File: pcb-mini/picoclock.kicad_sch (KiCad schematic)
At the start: 74 parts, among them J1 UART, J10 USB, J11 Alt Power, J12 LED_5V, J14 SJ2-35863B1-SMT-TR, J2 USB_A, J3 UART, J4 xx, J5 Micro_SD_Card_Det1, J6 USB_C_Receptacle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

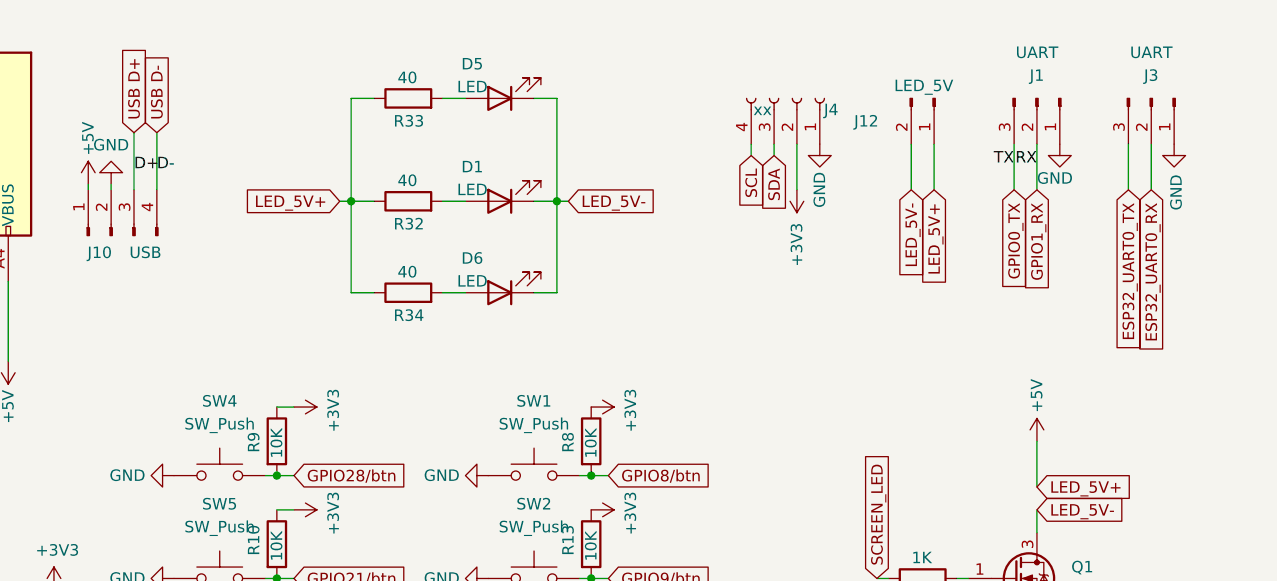
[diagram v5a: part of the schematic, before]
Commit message: [pcb] mini: add RGB leds
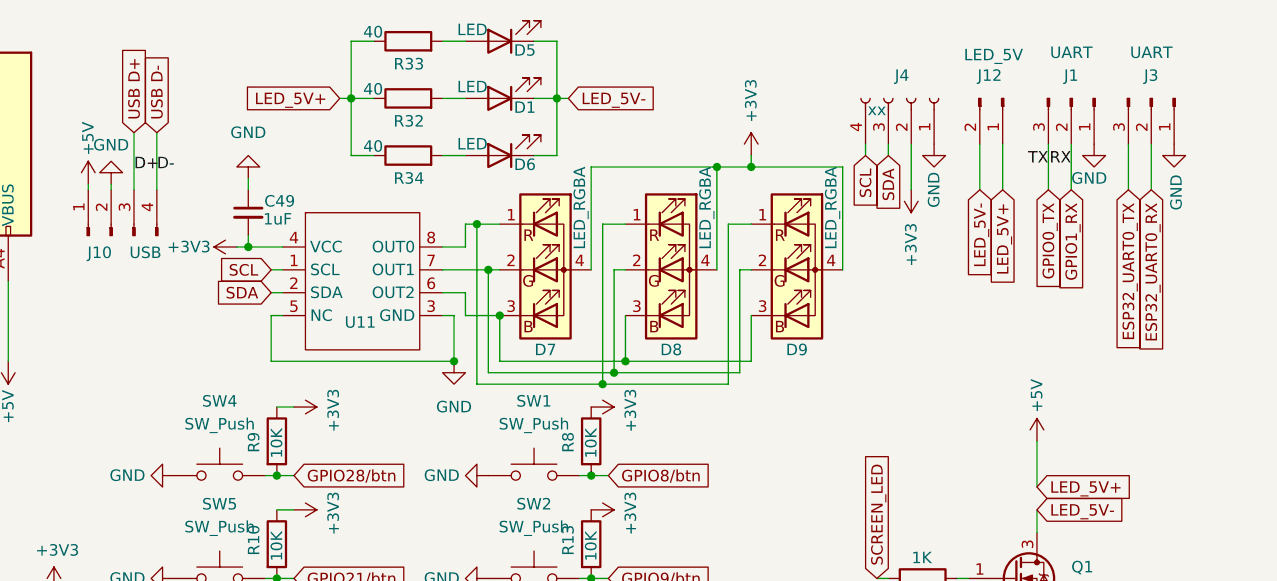
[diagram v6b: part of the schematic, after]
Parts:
- added C49: 1uF, Capacitor_SMD:C_0603_1608Metric, symbol Device:C_Small
- added D7, D8, D9: LED_RGBA, Resistor_SMD:R_Array_Convex_2x0606, symbol Device:LED_RGBA
- added U11: ~, Lunasys_Library:LP5817, symbol Lunasys_Library:LP5817
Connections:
- net +3V3: now also C49.2, D7.4 (A), D8.4 (A), D9.4 (A), U11.4 (VCC)
- net GND: now also C49.1, U11.3 (GND), U11.5 (NC)
- net SCL: now also U11.1 (SCL)
- net SDA: now also U11.2 (SDA)
- new net: D7.1 (RK), D8.1 (RK), D9.1 (RK), U11.8 (OUT0)
- new net: D7.2 (GK), D8.2 (GK), D9.2 (GK), U11.7 (OUT1)
- new net: D7.3 (BK), D8.3 (BK), D9.3 (BK), U11.6 (OUT2)
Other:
- moved on the sheet: D1, D5, D6, J1, J12, J4, R32, R33, R34

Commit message: [pcb] mini: fix I2S switch footprint, many small tweaks
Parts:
- U10: footprint Package_SO:TSSOP-16_4.4x5mm_P0.65mm -> Package_SO:SOIC-16_3.9x9.9mm_P1.27mm
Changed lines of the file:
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@@
 			)
 		)
-		(property "Description" "RGB LED, red/green/blue/anode"
+		(property "Description" "LTST-C19HE1WT"
+			(at 179.07 40.64 0)
+			(effects
+				(font
+					(size 1.27 1.27)
+				)
+				(hide yes)
+			)
+		)
+		(property "Field5" ""
 			(at 179.07 40.64 0)
 			(effects
@@
 			)
 		)
-		(property "Description" "RGB LED, red/green/blue/anode"
+		(property "Description" "LTST-C19HE1WT"
 			(at 165.1 40.64 0)
 			(effects
@@
 			)
 		)
-		(property "Description" "RGB LED, red/green/blue/anode"
+		(property "Description" "LTST-C19HE1WT"
 			(at 193.04 40.64 0)
 			(effects
@@
 			)
 		)
-		(property "Footprint" "Package_SO:TSSOP-16_4.4x5mm_P0.65mm"
+		(property "Footprint" "Package_SO:SOIC-16_3.9x9.9mm_P1.27mm"
 			(at 148.59 113.03 0)
 			(effects

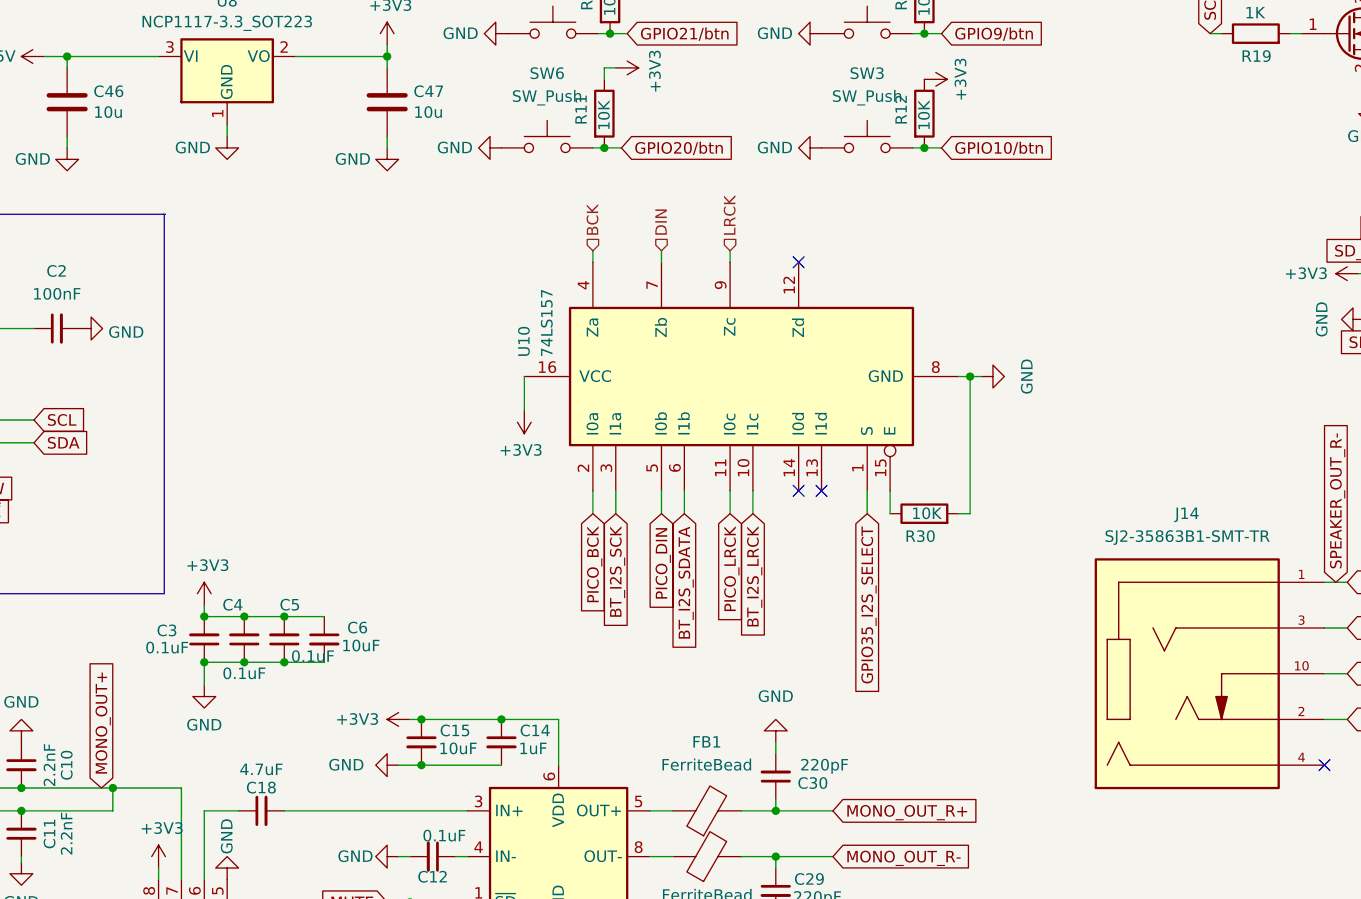
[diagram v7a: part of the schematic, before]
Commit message: [pcb] mini: add ENS160 gaz sensor
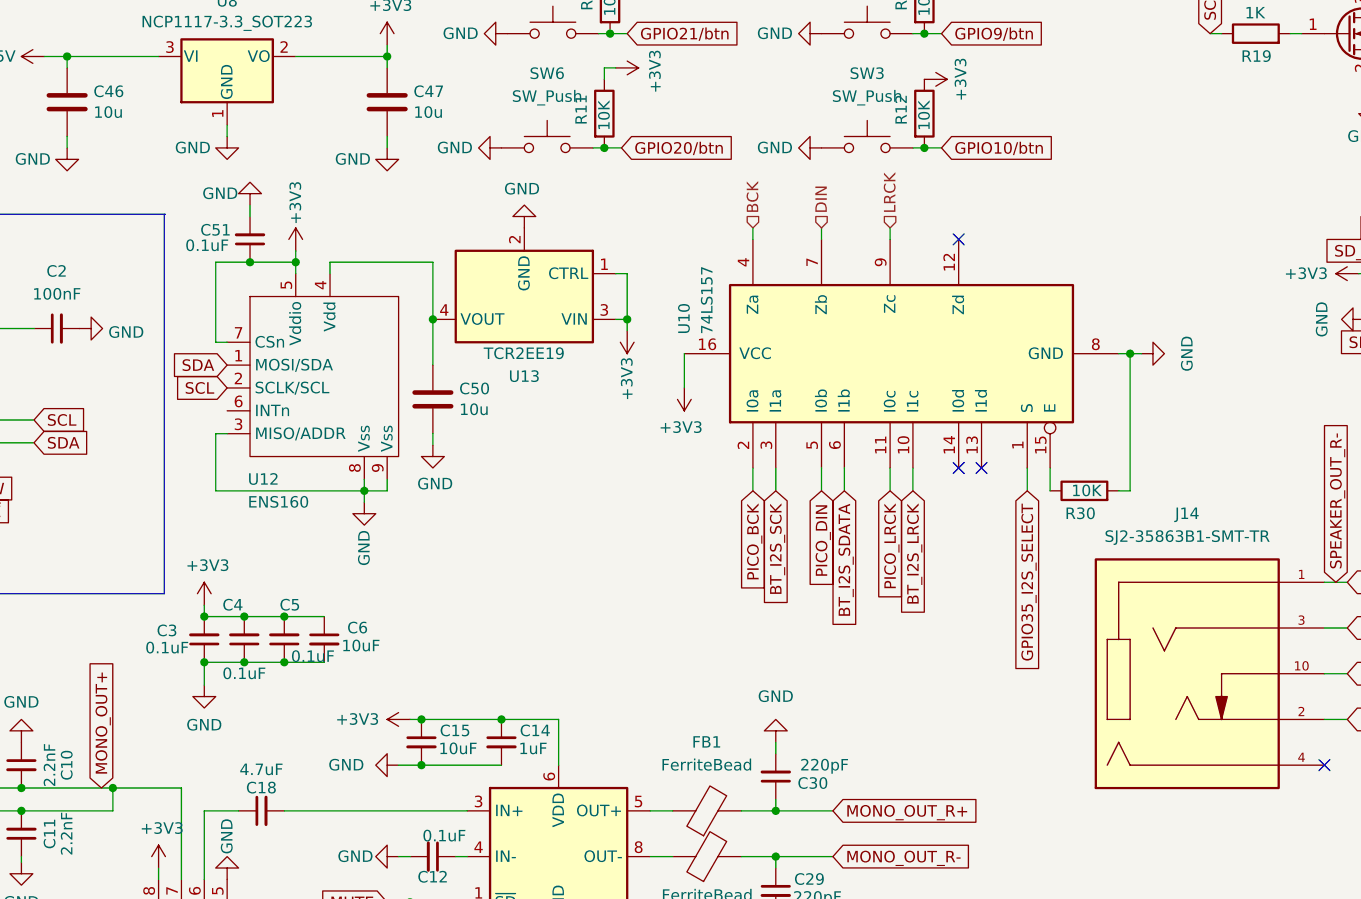
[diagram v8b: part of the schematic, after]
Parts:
- added C50: 10u, Capacitor_SMD:C_0805_2012Metric, symbol Device:C
- added C51: 0.1uF, Capacitor_SMD:C_0603_1608Metric, symbol Device:C_Small
- added U12: ENS160, ENS160:ENS160, symbol ENS160:ENS160
- added U13: TCR2EE19, Package_TO_SOT_SMD:SOT-23-5_HandSoldering, symbol Regulator_Linear:TCR2EE19
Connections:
- net +3V3: now also C51.1, U12.5 (Vddio), U12.7 (CSn), U13.1 (CTRL), U13.3 (VIN)
- net GND: now also C50.2, C51.2, U12.3 (MISO/ADDR), U12.8 (Vss), U12.9 (Vss), U13.2 (GND)
- net SCL: now also U12.2 (SCLK/SCL)
- net SDA: now also U12.1 (MOSI/SDA)
- new net: C50.1, U12.4 (Vdd), U13.4 (VOUT)
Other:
- moved on the sheet: R30, U10
